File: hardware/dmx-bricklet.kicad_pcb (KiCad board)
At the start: 2 copper layers, 38 parts, among them P1 CON-SENSOR2, P2 BOOT, P3 DMXCON_2x3, SW1 TER, U1 XMC1XXX48, U2 DRILL, U3 DRILL, U4 DRILL, U5 DRILL, U6 ADM3485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

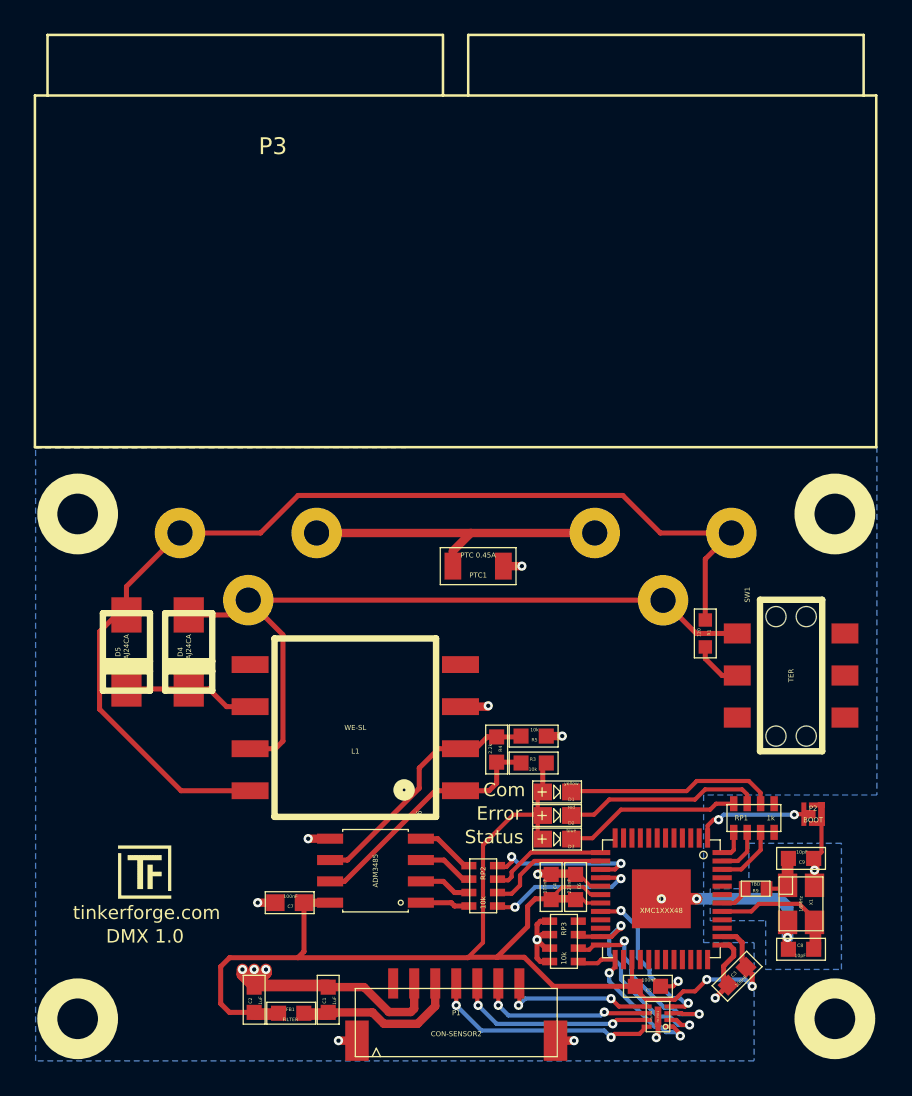
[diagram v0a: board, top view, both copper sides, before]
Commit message: Remove PTC1
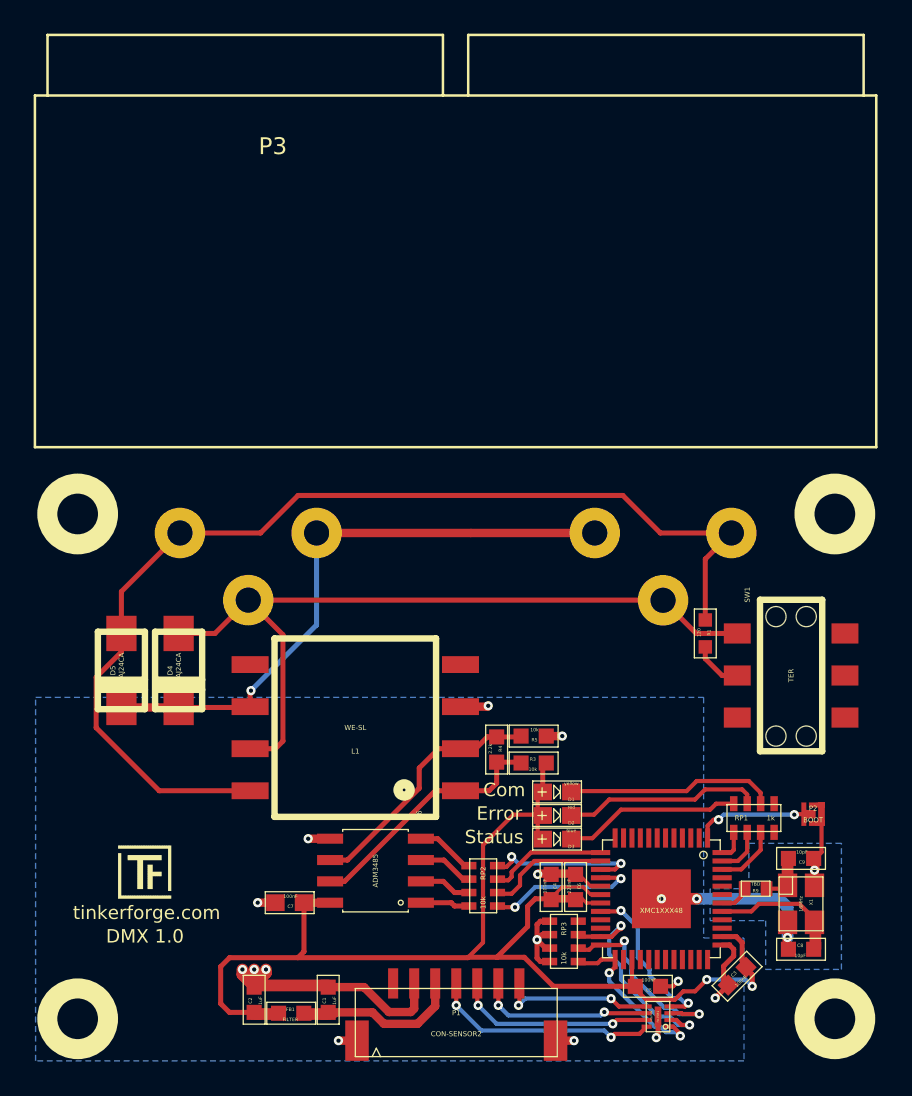
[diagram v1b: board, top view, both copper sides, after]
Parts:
- removed PTC1: PTC 0.45A, 1206
- moved D4 1.25 mm to (131.6, 97.8)
- moved D5 1.14 mm to (128.2, 97.8)
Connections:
- L1 pad 4: Net-(L1-Pad4) -> (no net)
- L1 pad 5: Net-(L1-Pad5) -> (no net)
- P3 pad 1: Net-(P3-Pad1) -> Net-(D4-Pad2)
- P3 pad 4: Net-(P3-Pad1) -> Net-(D4-Pad2)
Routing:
- net Net-(D4-Pad2): track 7.78 -> 36.2 mm, vias 0 -> 1
- net Net-(P3-Pad1): track 18.9 -> 0.00 mm
- net Net-(D4-Pad1): track 45.2 -> 47.5 mm
- net GND: track 57.0 -> 55.9 mm, vias 19 -> 18
- net Net-(D5-Pad1): track 64.1 -> 64.7 mm

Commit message: Add WEEE and CE logos
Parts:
- added G***: LOGO, kicad-libraries:WEEE_7mm, B.Cu at (153.1, 97.1)
- added G***: LOGO, kicad-libraries:Logo_CoMCU, B.Cu at (129.5, 104.4)
- added VAL: CE_5mm, kicad-libraries:CE_5mm, B.Cu at (143.1, 97.1)

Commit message: Fix CE logo
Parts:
- turned VAL to 180 degrees
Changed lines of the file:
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@@
   )
   (module kicad-libraries:CE_5mm (layer Rückseite)
-    (at 143.11 97.13)
-    (fp_text reference VAL (at 0 0) (layer B.SilkS) hide
+    (at 143.11 97.13 180)
+    (fp_text reference VAL (at 0 0 180) (layer B.SilkS) hide
       (effects (font (size 1.143 1.143) (thickness 0.1778)) (justify mirror))
     )
-    (fp_text value CE_5mm (at 0 0) (layer B.SilkS) hide
+    (fp_text value CE_5mm (at 0 0 180) (layer B.SilkS) hide
       (effects (font (size 1.143 1.143) (thickness 0.1778)) (justify mirror))
     )

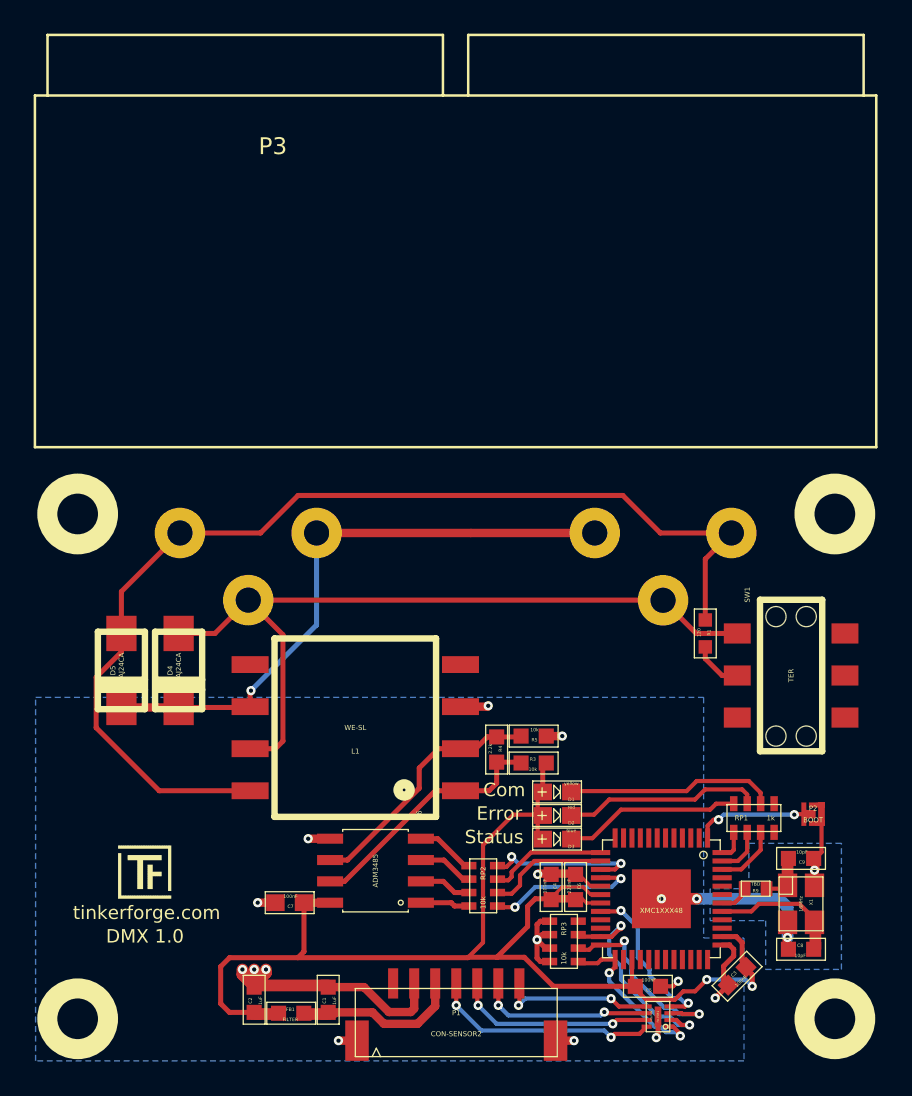
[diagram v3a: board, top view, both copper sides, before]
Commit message: Change filtering to R/C circuit
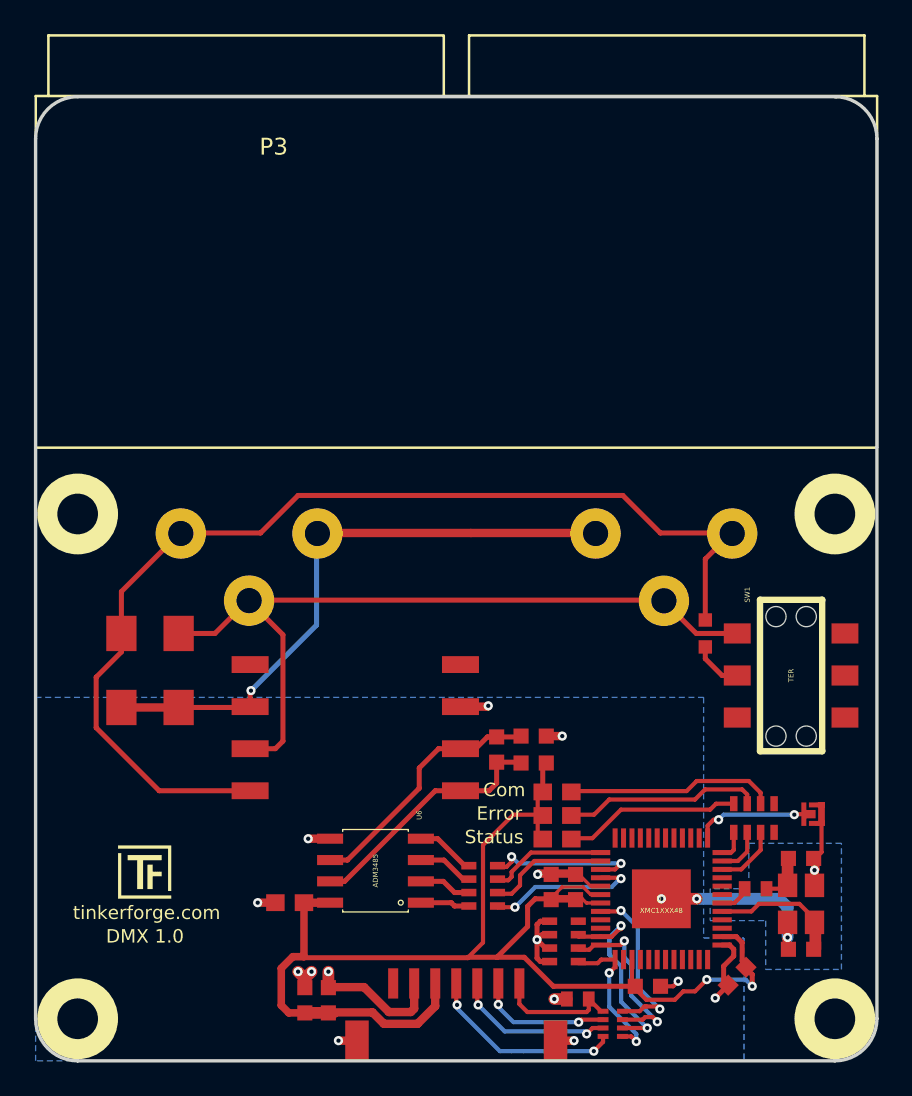
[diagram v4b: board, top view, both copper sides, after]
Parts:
- removed FB1: FILTER, 0603F
- removed FILTER1: Filter-4x, kicad-libraries:DFN8-17x135
- added C10: TBD, kicad-libraries:C0402E, F.Cu at (155.3, 117.4)
- added RP4: TBD, kicad-libraries:4X0402, F.Cu at (157.4, 118.8)
- C1, C2, C3, C4, C5, C6, C8, C9: footprint 0603F -> kicad-libraries:C0603F
- C7: footprint 0603E -> kicad-libraries:C0603E
- D1, D2, D3: footprint D0603E -> kicad-libraries:D0603E
- D4, D5: footprint DO-214AC -> kicad-libraries:DO-214AC
- L1: footprint WE-SL -> kicad-libraries:WE-SL
- P1: footprint CON-SENSOR2 -> kicad-libraries:CON-SENSOR2
- P3: footprint DMX_IN_OUT_2x3POL -> kicad-libraries:DMX_IN_OUT_2x3POL
- R1: footprint 0603 -> kicad-libraries:R0603
- R3, R4, R5: footprint 0603F -> kicad-libraries:R0603F
- R9: footprint 0402E -> kicad-libraries:R0402E
- U2, U3, U4, U5: footprint DRILL_NP -> kicad-libraries:DRILL_NP
- U6: footprint SOIC8 -> kicad-libraries:SOIC8
- moved G*** 30.1 mm to (135.4, 74.9)
- moved G*** 23.5 mm to (160.7, 74.9)
- moved VAL 22.8 mm to (148.1, 74.9), turned to 0 degrees
- moved P3 13.1 mm to (148.1, 60.1)
- moved C2 3.01 mm to (139.1, 117.4)
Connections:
- C1 pad 2: Net-(C1-Pad2) -> VCC
- P1 pad 3: Net-(C1-Pad2) -> VCC
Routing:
- net Net-(C1-Pad2): track 10.1 -> 0.00 mm
- net GND: track 55.9 -> 50.1 mm
- net VCC: track 77.7 -> 82.3 mm
- net Net-(P1-Pad6): track 10.5 -> 8.06 mm
- net Net-(P1-Pad5): track 11.9 -> 9.58 mm
- net Net-(C10-Pad1): track 9.30 -> 7.40 mm, vias 2 -> 0
- net Net-(P1-Pad4): track 13.7 -> 11.8 mm
- net S-CS: track 10.2 -> 8.91 mm
- net S-MOSI: track 11.9 -> 11.4 mm
- net S-CLK: track 13.2 -> 12.7 mm
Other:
- board outline added: 50 x 57.3 mm

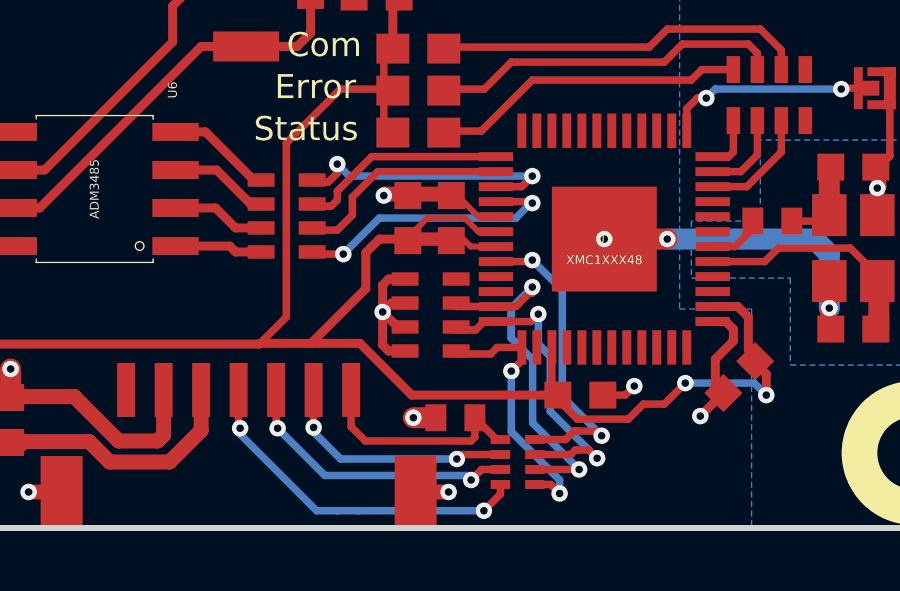
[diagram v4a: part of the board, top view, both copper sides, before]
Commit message: Remove RP3
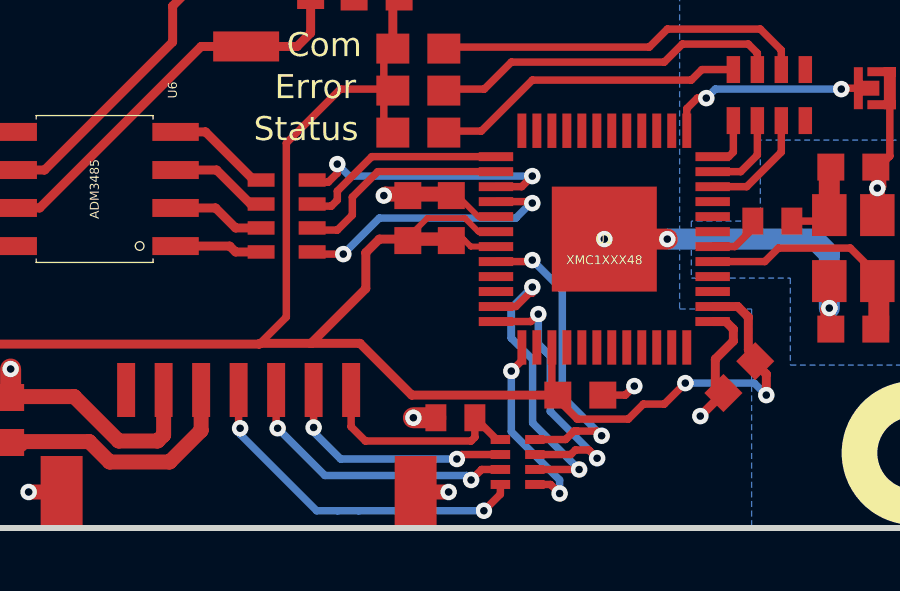
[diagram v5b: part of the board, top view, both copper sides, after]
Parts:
- removed RP3: 10k, kicad-libraries:0603X4
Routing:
- net GND: track 50.1 -> 44.6 mm, vias 18 -> 17
- net S-CS: track 8.91 -> 6.63 mm
- net S-CLK: track 12.7 -> 11.4 mm
- net S-MOSI: track 11.4 -> 10.3 mm

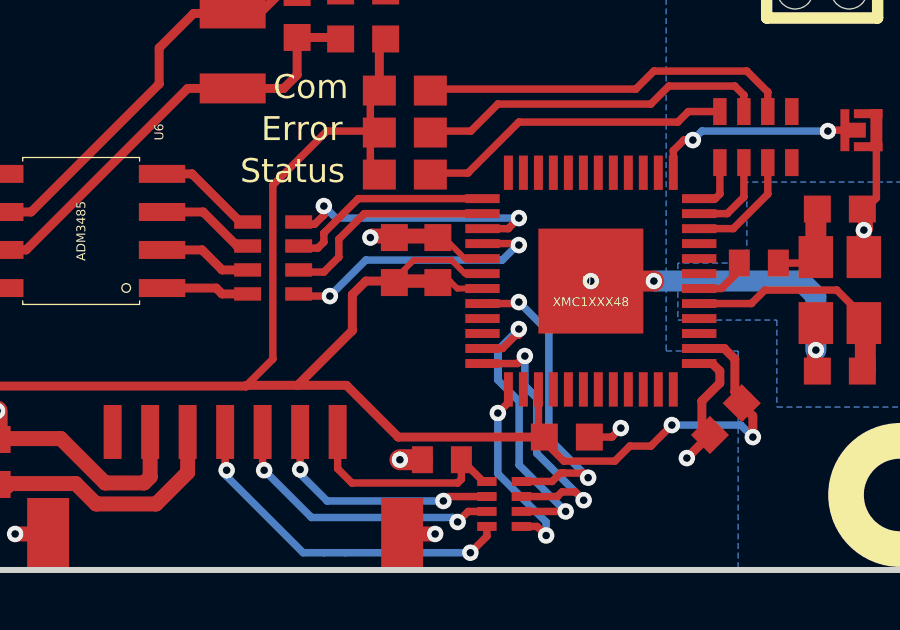
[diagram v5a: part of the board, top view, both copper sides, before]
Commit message: change rx pin connection to p3.0
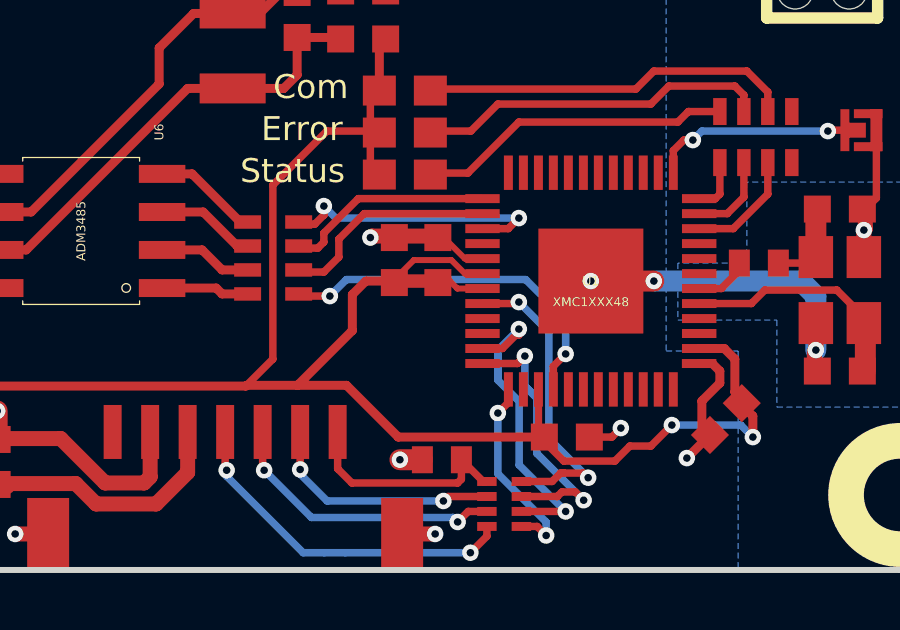
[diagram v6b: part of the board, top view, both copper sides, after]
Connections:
- P1 pad 1: Net-(P1-Pad1) -> (no net)
- RP1 pad 1: Net-(RP1-Pad1) -> (no net)
- RP1 pad 8: Net-(RP1-Pad8) -> (no net)
- SW1 pad 3: Net-(SW1-Pad3) -> (no net)
- SW1 pad 4: Net-(SW1-Pad4) -> (no net)
- SW1 pad 5: Net-(SW1-Pad5) -> (no net)
- SW1 pad 6: Net-(SW1-Pad6) -> (no net)
- U1 pad 10: Net-(U1-Pad10) -> (no net)
- U1 pad 11: Net-(U1-Pad11) -> (no net)
- U1 pad 12: Net-(U1-Pad12) -> (no net)
- U1 pad 16: 485-RX -> (no net)
- U1 pad 2: Net-(U1-Pad2) -> (no net)
- U1 pad 21: Net-(U1-Pad21) -> (no net)
- U1 pad 22: Net-(U1-Pad22) -> (no net)
- U1 pad 26: Net-(U1-Pad26) -> (no net)
- U1 pad 28: Net-(U1-Pad28) -> 485-RX
- U1 pad 29: Net-(U1-Pad29) -> (no net)
- U1 pad 3: Net-(U1-Pad3) -> (no net)
- U1 pad 30: Net-(U1-Pad30) -> (no net)
- U1 pad 31: Net-(U1-Pad31) -> (no net)
- U1 pad 32: Net-(U1-Pad32) -> (no net)
- U1 pad 33: Net-(U1-Pad33) -> (no net)
- U1 pad 34: Net-(U1-Pad34) -> (no net)
- U1 pad 35: Net-(U1-Pad35) -> (no net)
- U1 pad 36: Net-(U1-Pad36) -> (no net)
- U1 pad 39: Net-(U1-Pad39) -> (no net)
- U1 pad 4: Net-(U1-Pad4) -> (no net)
- U1 pad 40: Net-(U1-Pad40) -> (no net)
- U1 pad 43: Net-(U1-Pad43) -> (no net)
- U1 pad 44: Net-(U1-Pad44) -> (no net)
- U1 pad 45: Net-(U1-Pad45) -> (no net)
- U1 pad 5: Net-(U1-Pad5) -> (no net)
- U1 pad 6: Net-(U1-Pad6) -> (no net)
- U1 pad 7: Net-(U1-Pad7) -> (no net)
- U1 pad 8: Net-(U1-Pad8) -> (no net)
- U1 pad 9: Net-(U1-Pad9) -> (no net)
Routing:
- net 485-RX: track 9.29 -> 12.2 mm
